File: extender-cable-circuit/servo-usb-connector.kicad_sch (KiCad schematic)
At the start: 12 parts

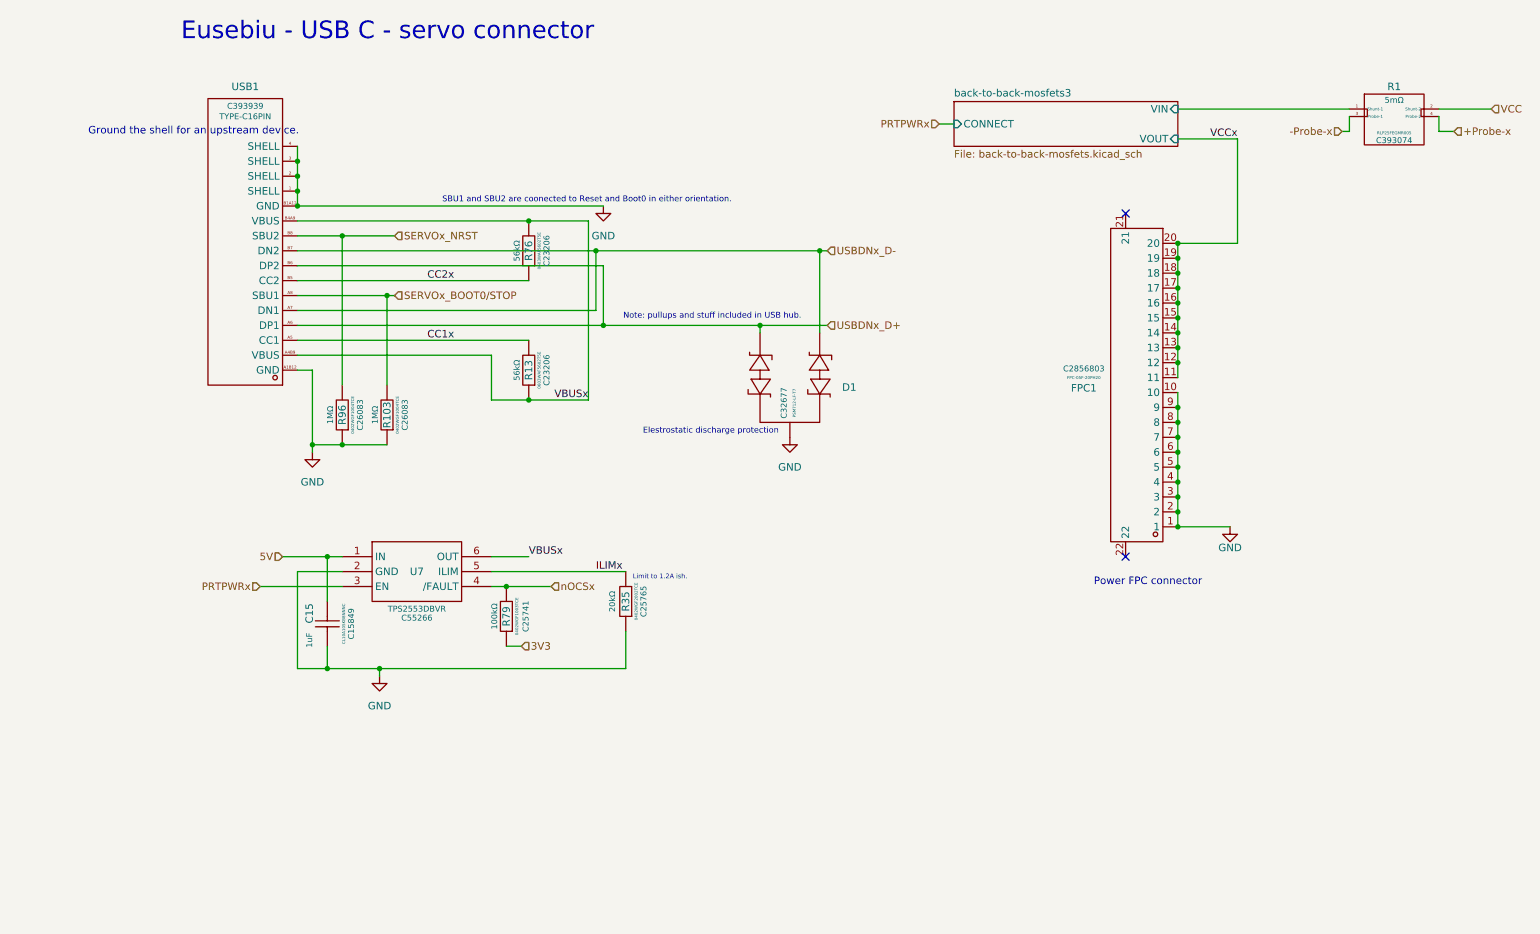
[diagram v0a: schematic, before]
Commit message: Make schematic for the cable plug and extension circuit.
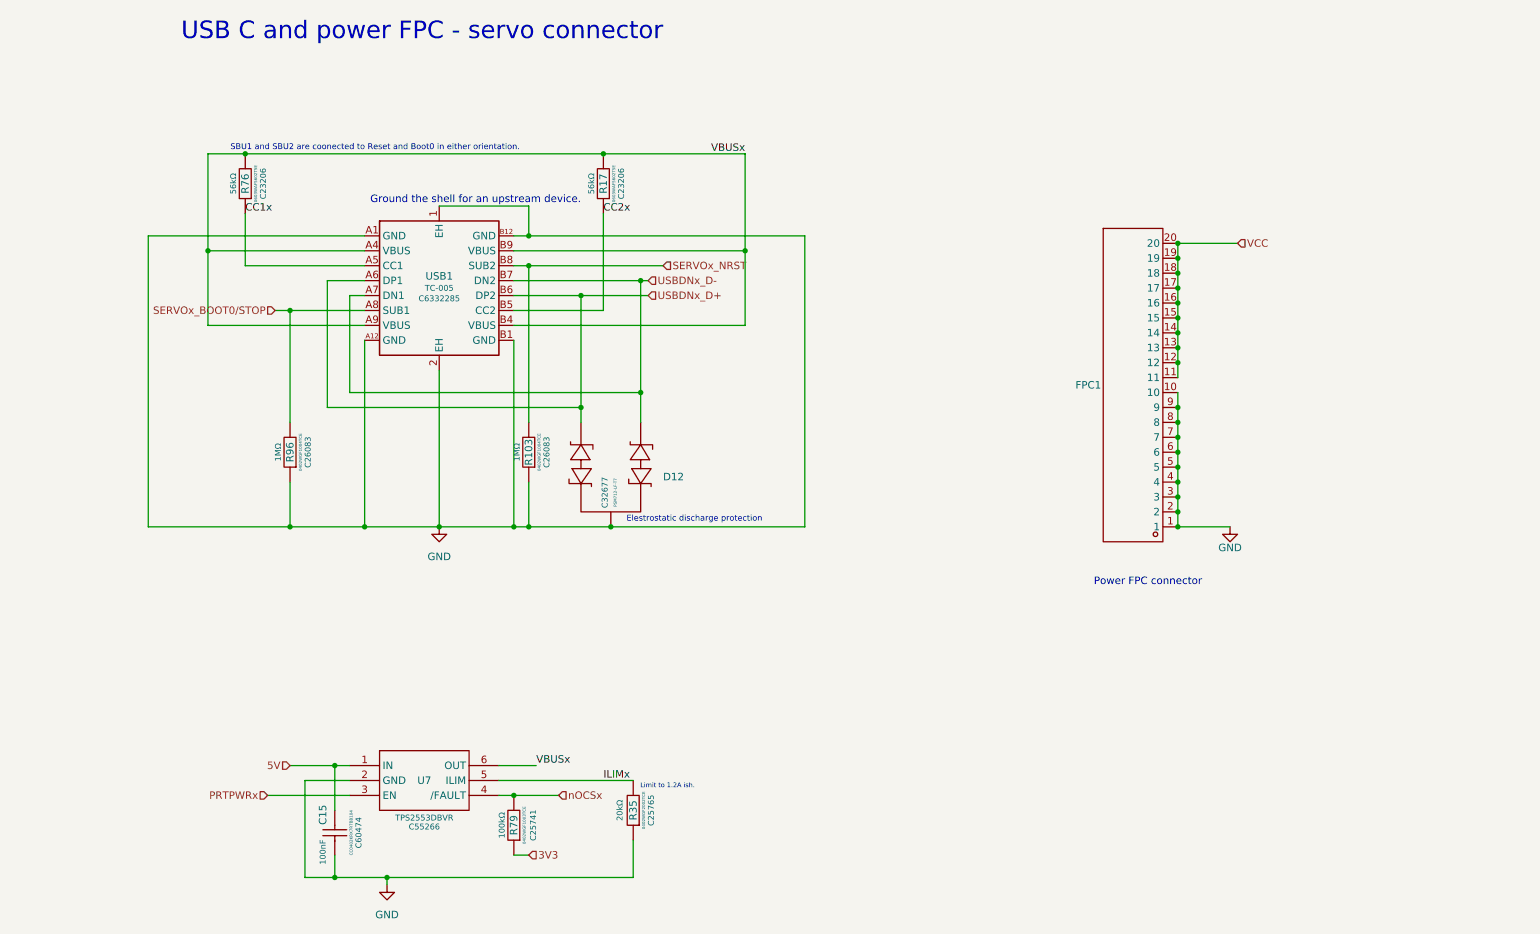
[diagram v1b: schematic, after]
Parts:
- removed C15: 1uF, Library:C0603, symbol Library:CL10A105KB8NNNC Capacitor 1uF
- removed D1: (no value), Library:SOT-23-3_L3.0-W1.7-P0.95-LS2.9-BR, symbol Library:PSM712-LF-T7 ETV/ESD Diodes
- removed FPC1: (no value), Library:FPC-SMD_20P-P0.50_XUNPU_FPC-05F-20PH20, symbol Library:FPC-05F-20PH20 Connector 20P 0.5mm spacing FPC
- removed R1: 5mΩ, Library:R2512 Shunt with Kelvin connections, symbol Library:RLP25FEGMR005 Shunt resistor 5mΩ 1%
- removed R13: 56kΩ, Library:R0603, symbol Library:0603WAF5602T5E Resistor 56kΩ
- removed USB1: (no value), Library:USB-C-SMD_TYPE-C16PIN, symbol Library:TYPE-C16PIN USB connector
- added C15: 100nF, Library:C0402, symbol Library:CC0402KRX7R7BB104 Capacitor 100nF
- added D12: (no value), Library:SOT-23-3_L3.0-W1.7-P0.95-LS2.9-BR, symbol Library:PSM712-LF-T7 ETV/ESD Diodes
- added FPC1: (no value), Library:FPC-20P-P0.50-Pattern, symbol Library:FPC-05F-6PH20 Pattern 20P 0.5mm spacing
- added R17: 56kΩ, Library:R0603, symbol Library:0603WAF5602T5E Resistor 56kΩ
- added USB1: (no value), Library:USB-C-SMD_TC-005, symbol Library:TC-005_C6332285 male USB-C plug
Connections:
- net 5V: now also C15.2
- net CC1x: now also R76.1, USB1.A5 (CC1)
- net CC2x: now also R17.1, USB1.B5 (CC2); no longer R76.1
- net GND: now also C15.1, D12.3 (K), FPC1.1, FPC1.10, FPC1.2, FPC1.3, FPC1.4, FPC1.5, FPC1.6, FPC1.7, FPC1.8, FPC1.9, USB1.1 (EH), USB1.2 (EH), USB1.A1 (GND), USB1.A12 (GND), USB1.B1 (GND), USB1.B12 (GND)
- net SERVOx_BOOT0/STOP: now also R96.2, USB1.A8 (SUB1); no longer R103.2
- net SERVOx_NRST: now also R103.2, USB1.B8 (SUB2); no longer R96.2
- net USBDNx_D+: now also D12.2 (A1), USB1.A6 (DP1), USB1.B6 (DP2)
- net USBDNx_D-: now also D12.1 (A1), USB1.A7 (DN1), USB1.B7 (DN2)
- net VBUSx: now also R17.2, USB1.A4 (VBUS), USB1.A9 (VBUS), USB1.B4 (VBUS), USB1.B9 (VBUS)
- net VCC: now also FPC1.11, FPC1.12, FPC1.13, FPC1.14, FPC1.15, FPC1.16, FPC1.17, FPC1.18, FPC1.19, FPC1.20
- no-connect marks 2 -> 0
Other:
- removed sheet back-to-back-mosfets3
- note added: "USB C and power FPC - servo connector"
- note removed: "Eusebiu - USB C - servo connector"
- note removed: "Note: pullups and stuff included in USB hub."
- moved on the sheet: R35, R79, U7

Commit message: Working on rally compact layout for cable extender.
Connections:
- net 5V renamed VBUS
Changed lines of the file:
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@@
 		)
 	)
-	(hierarchical_label "5V"
+	(hierarchical_label "VBUS"
 		(shape input)
 		(at 64.77 153.67 180)
